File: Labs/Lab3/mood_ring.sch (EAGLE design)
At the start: 8 parts

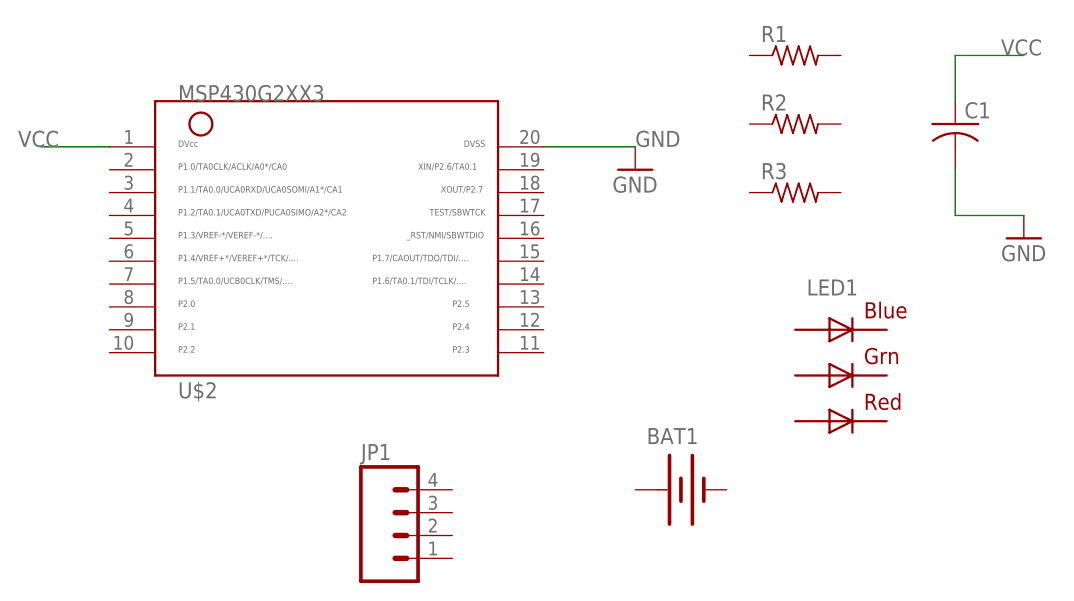
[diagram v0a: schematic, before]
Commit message: Added Labs directory, changed Lab2 to Lab3 and added datasheets
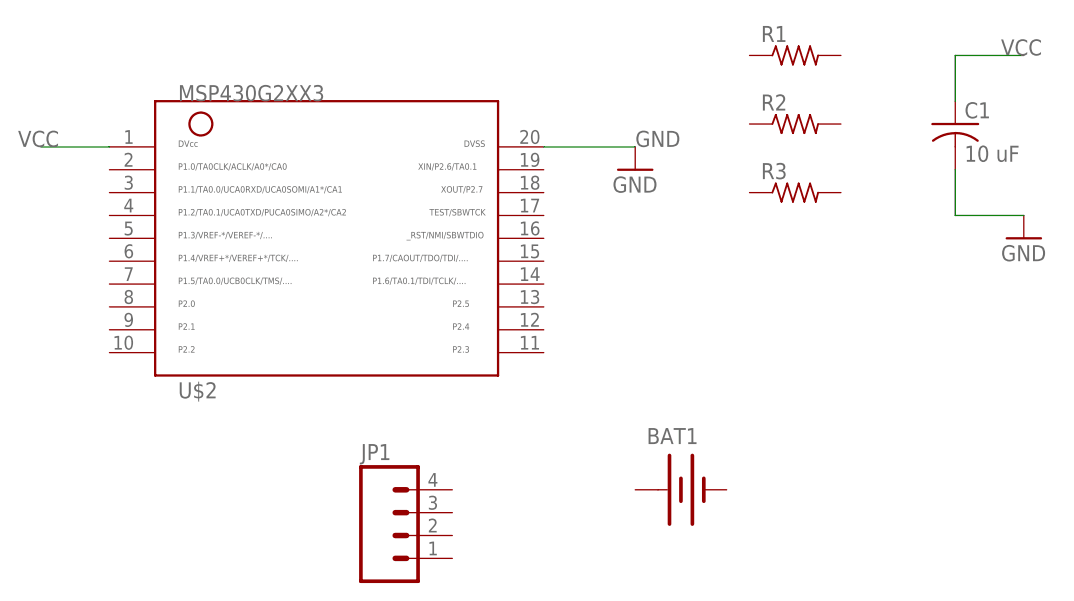
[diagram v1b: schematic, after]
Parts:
- removed LED1: RGBLED5050, adafruit:RGBLED5050
- C1: value (none) -> 10 uF
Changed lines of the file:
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@@
 <?xml version="1.0" encoding="utf-8"?>
 <!DOCTYPE eagle SYSTEM "eagle.dtd">
-<eagle version="6.5.0">
+<eagle version="7.3.0">
 <drawing>
 <settings>
@@
 <part name="R2" library="resistor" deviceset="R-US_" device="R1206"/>
 <part name="R3" library="resistor" deviceset="R-US_" device="R1206"/>
-<part name="LED1" library="adafruit" deviceset="RGBLED" device="5050"/>
 <part name="BAT1" library="ELEC327" deviceset="BATTERY" device="BU2032SM"/>
-<part name="C1" library="resistor" deviceset="C-US" device="C1206"/>
+<part name="C1" library="resistor" deviceset="C-US" device="C1206" value="10 uF"/>
 <part name="GND1" library="supply1" deviceset="GND" device=""/>
 <part name="GND2" library="supply1" deviceset="GND" device=""/>
@@
 <instance part="R2" gate="G$1" x="27.94" y="182.88"/>
 <instance part="R3" gate="G$1" x="27.94" y="175.26"/>
-<instance part="LED1" gate="G$1" x="33.02" y="154.94"/>
 <instance part="BAT1" gate="G$1" x="15.24" y="142.24"/>
 <instance part="C1" gate="G$1" x="45.72" y="182.88"/>
